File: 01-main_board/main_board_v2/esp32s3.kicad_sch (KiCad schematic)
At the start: 28 parts, among them IC10 ESP32-S3, Y1 ECS-400-10-37B2-CKY-TR, Y2 ECS-.327-12.5-34B-TR

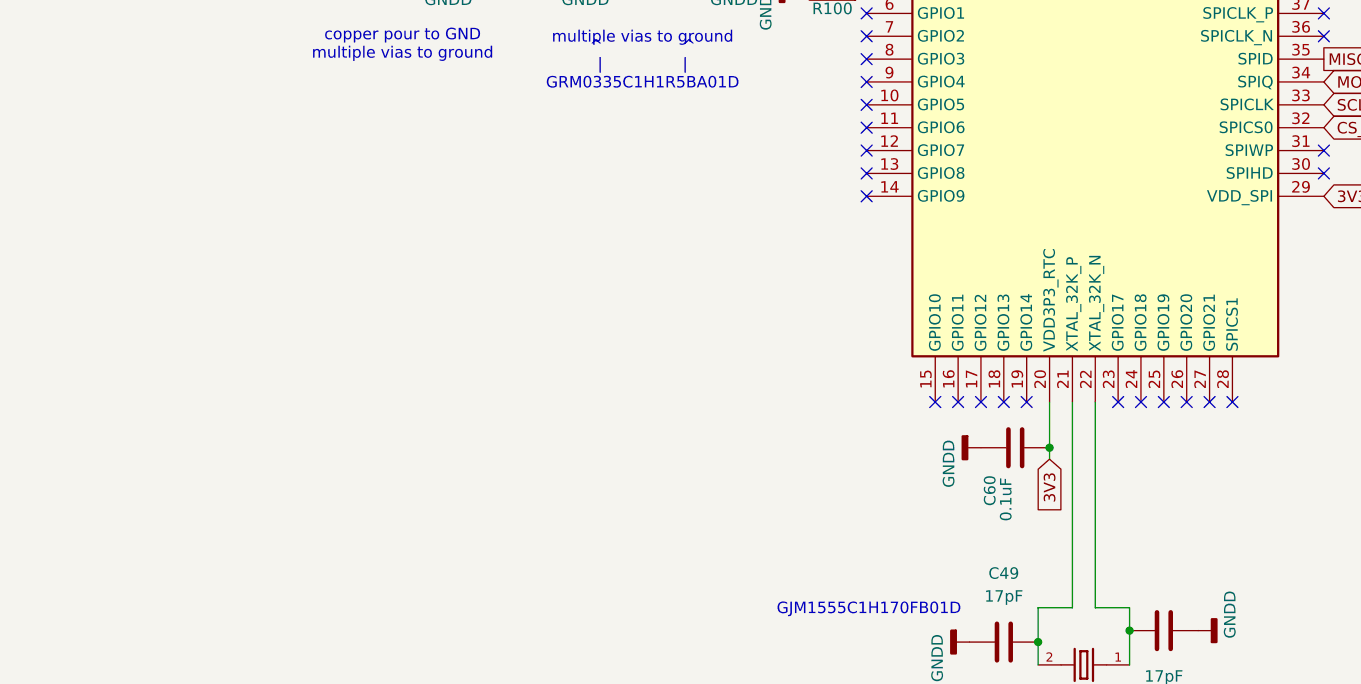
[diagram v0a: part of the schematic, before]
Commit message: added usb mux
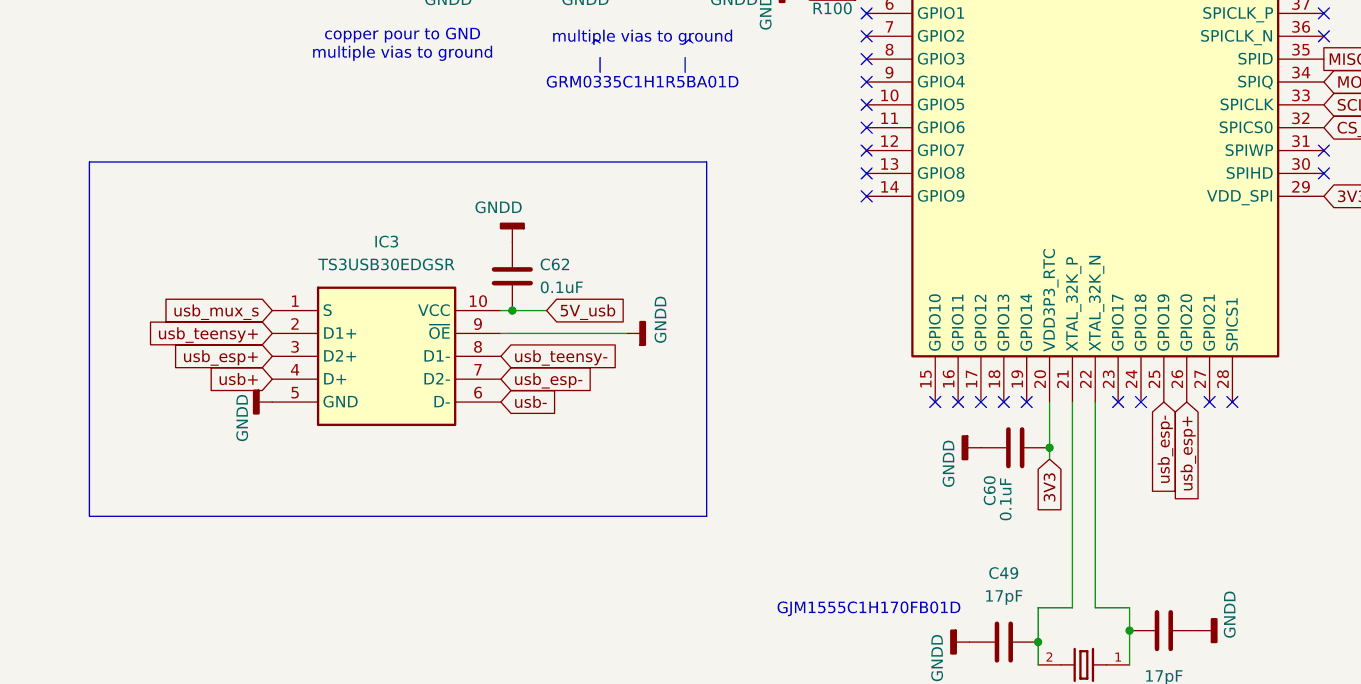
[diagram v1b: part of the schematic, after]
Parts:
- added C62: 0.1uF, Capacitor_SMD:C_0603_1608Metric, symbol Device:C
- added IC3: TS3USB30EDGSR, SOP50P490X110-10N, symbol 22XT_Main_v2:TS3USB30EDGSR
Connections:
- net GNDD: now also C62.1, IC3.5 (GND), IC3.9 (~{OE})
- net usb_esp-: now reaches IC10.25 (GPIO19)
- net usb_esp-: now also IC3.7 (D2-)
- net usb_esp+: now reaches IC10.26 (GPIO20)
- net usb_esp+: now also IC3.3 (D2+)
- new net 5V_usb: C62.2, IC3.10 (VCC)
- new net usb+: IC3.4 (D+)
- new net usb-: IC3.6 (D-)
- new net usb_mux_s: IC3.1 (S)
- new net usb_teensy+: IC3.2 (D1+)
- new net usb_teensy-: IC3.8 (D1-)
- no-connect marks 38 -> 36

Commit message: finished sensor input layout and some spi bus
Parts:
- C62: footprint Capacitor_SMD:C_0603_1608Metric -> Capacitor_SMD:C_0402_1005Metric
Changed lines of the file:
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@@
 			)
 		)
-		(property "Footprint" "Capacitor_SMD:C_0603_1608Metric"
+		(property "Footprint" "Capacitor_SMD:C_0402_1005Metric"
 			(at 82.2452 129.54 0)
 			(effects

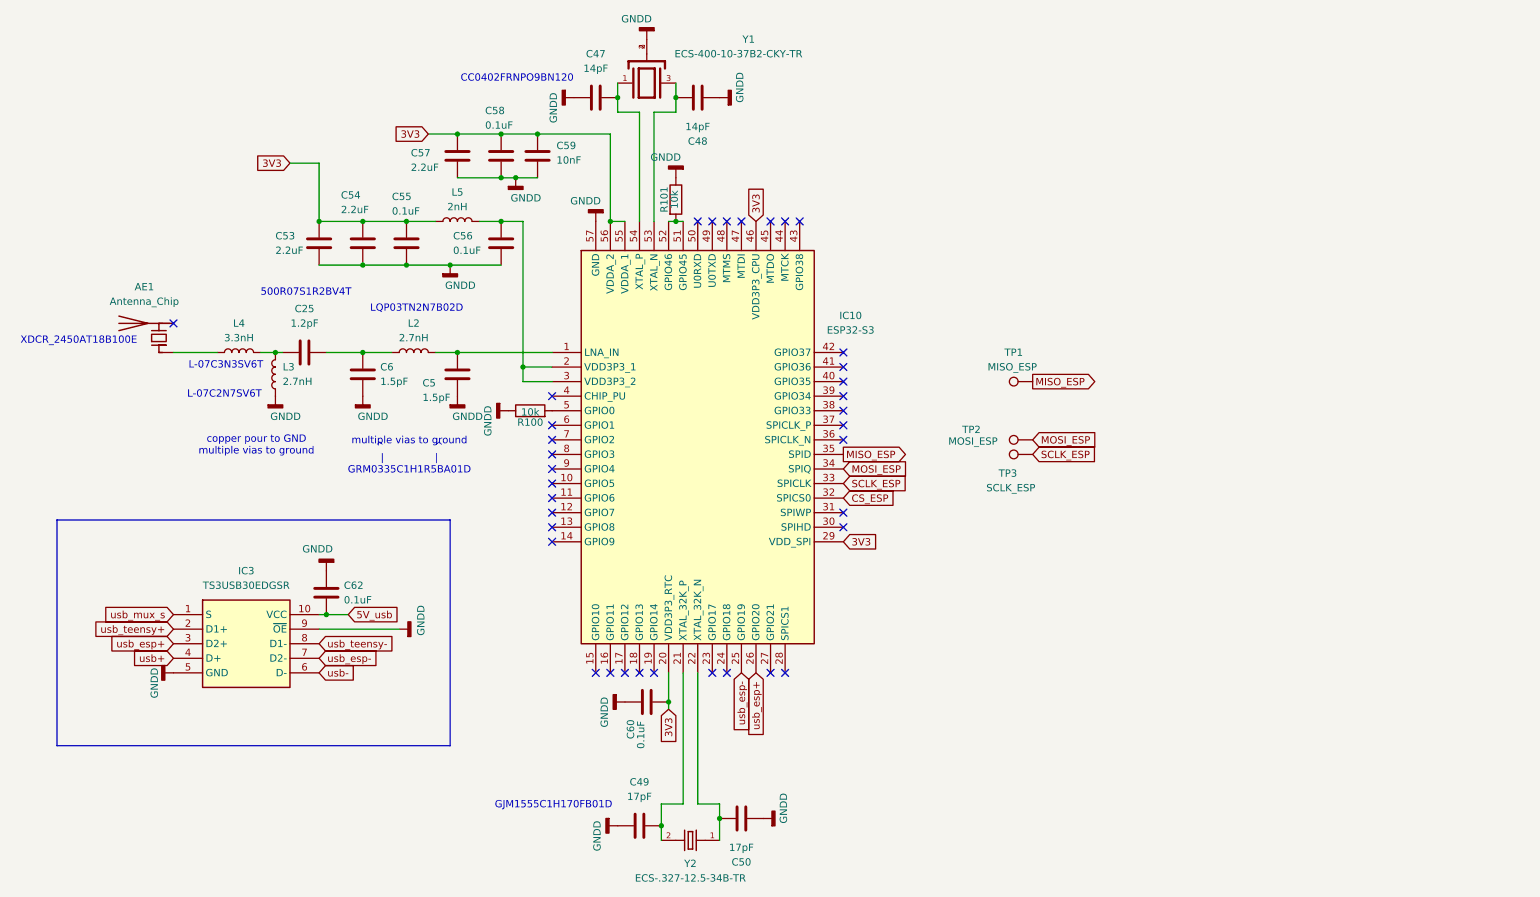
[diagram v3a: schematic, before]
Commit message: finished layout, resolved drc errors, need to resolve warnings and get checked
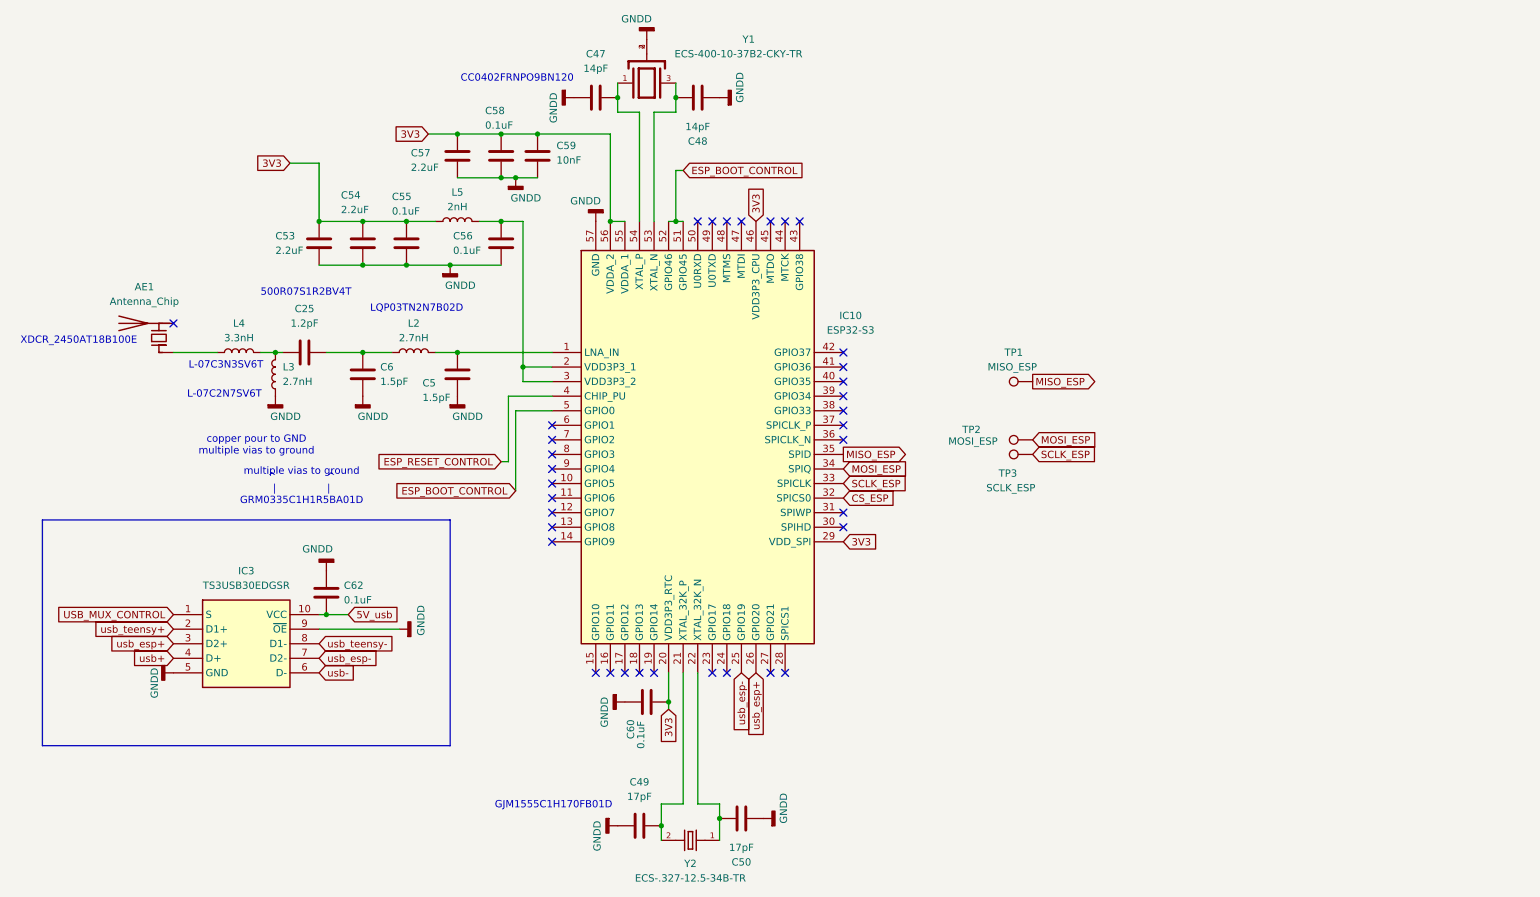
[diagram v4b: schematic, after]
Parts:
- removed R100, R101: 10k, Resistor_SMD:R_0402_1005Metric, symbol Device:R
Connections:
- net ESP_BOOT_CONTROL: now reaches IC10.5 (GPIO0)
- net ESP_BOOT_CONTROL: now also IC10.51 (GPIO45), IC10.52 (GPIO46)
- net ESP_RESET_CONTROL: now reaches IC10.4 (CHIP_PU)
- net usb_mux_s renamed USB_MUX_CONTROL
- no-connect marks 36 -> 35

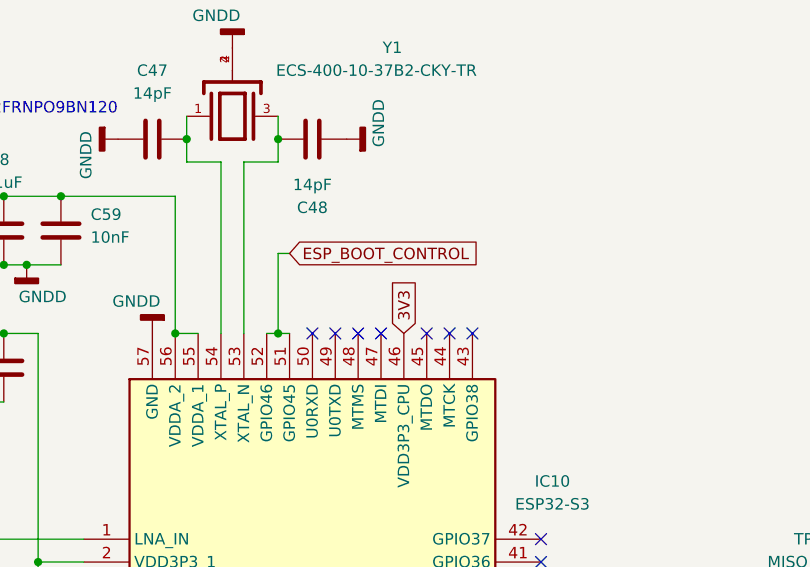
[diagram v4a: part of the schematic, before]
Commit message: resolved silkscreen issues, tied gpio45 to gnd
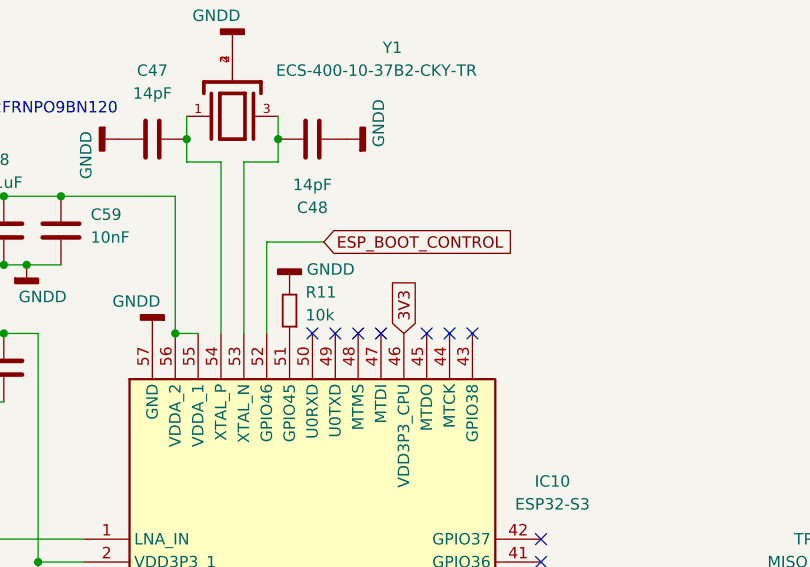
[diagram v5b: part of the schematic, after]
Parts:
- added R11: 10k, Resistor_SMD:R_0402_1005Metric, symbol Device:R_Small
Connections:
- net ESP_BOOT_CONTROL: no longer IC10.51 (GPIO45)
- net GNDD: now also R11.2
- new net: IC10.51 (GPIO45), R11.1
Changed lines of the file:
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@@
 	)
 	(junction
-		(at 142.24 60.96)
-		(diameter 0)
-		(color 0 0 0 0)
-	)
-	(junction
 		(at 104.14 83.82)
 		(diameter 0)
@@
 	(wire
 		(pts
-			(xy 142.24 60.96) (xy 143.51 60.96)
-		)
-		(stroke
-			(width 0)
-			(type default)
-		)
-	)
-	(wire
-		(pts
 			(xy 140.97 146.05) (xy 140.97 144.78)
 		)
@@
 	(wire
 		(pts
-			(xy 146.05 139.7) (xy 146.05 162.56)
-		)
-		(stroke
-			(width 0)
-			(type default)
-		)
-	)
-	(wire
-		(pts
-			(xy 115.57 86.36) (xy 120.65 86.36)
+			(xy 140.97 50.8) (xy 140.97 60.96)
 		)
 		(stroke
@@
 	(wire
 		(pts
-			(xy 143.51 139.7) (xy 143.51 162.56)
+			(xy 146.05 139.7) (xy 146.05 162.56)
 		)
 		(stroke
@@
 	(wire
 		(pts
-			(xy 142.24 60.96) (xy 142.24 52.07)
+			(xy 115.57 86.36) (xy 120.65 86.36)
 		)
 		(stroke
@@
 	(wire
 		(pts
-			(xy 140.97 60.96) (xy 142.24 60.96)
+			(xy 143.51 139.7) (xy 143.51 162.56)
 		)
 		(stroke
@@
 	(wire
 		(pts
-			(xy 142.24 52.07) (xy 143.51 52.07)
-		)
-		(stroke
-			(width 0)
-			(type default)
-		)
-	)
-	(wire
-		(pts
 			(xy 69.85 83.82) (xy 72.39 83.82)
 		)
@@
 	(wire
 		(pts
+			(xy 140.97 50.8) (xy 147.32 50.8)
+		)
+		(stroke
+			(width 0)
+			(type default)
+		)
+	)
+	(wire
+		(pts
 			(xy 149.86 168.91) (xy 149.86 165.1)
 		)
@@
 	(global_label "ESP_BOOT_CONTROL"
 		(shape input)
-		(at 143.51 52.07 0)
+		(at 147.32 50.8 0)
 		(fields_autoplaced yes)
 		(effects
@@
 		)
 		(property "Intersheetrefs" "${INTERSHEET_REFS}"
-			(at 165.4847 52.07 0)
+			(at 169.2947 50.8 0)
 			(effects
 				(font
@@
 	)
 	(symbol
+		(lib_id "Device:R_Small")
+		(at 143.51 58.42 180)
+		(unit 1)
+		(exclude_from_sim no)
+		(in_bom yes)
+		(on_board yes)
+		(dnp no)
+		(property "Reference" "R11"
+			(at 145.288 56.388 0)
+			(effects
+				(font
+					(size 1.27 1.27)
+				)
+				(justify right)
+			)
+		)
+		(property "Value" "10k"
+			(at 145.288 58.928 0)
+			(effects
+				(font
+					(size 1.27 1.27)
+				)
+				(justify right)
+			)
+		)
+		(property "Footprint" "Resistor_SMD:R_0402_1005Metric"
+			(at 143.51 58.42 0)
+			(effects
+				(font
+					(size 1.27 1.27)
+				)
+				(hide yes)
+			)
+		)
+		(property "Datasheet" "~"
+			(at 143.51 58.42 0)
+			(effects
+				(font
+					(size 1.27 1.27)
+				)
+				(hide yes)
+			)
+		)
+		(property "Description" "Resistor, small symbol"
+			(at 143.51 58.42 0)
+			(effects
+				(font
+					(size 1.27 1.27)
+				)
+				(hide yes)
+			)
+		)
+		(pin "1"
+		)
+		(pin "2"
+		)
+		(instances
+			(project "main_board_v2"
+				(path "/12c2237c-5932-49af-9119-92b28c846ae7/e5005576-746e-4110-9aa7-21d70d5867f0"
+					(reference "R11")
+					(unit 1)
+				)
+			)
+		)
+	)
+	(symbol
 		(lib_id "Device:C")
 		(at 135.89 166.37 270)
@@
 					(unit 1)
 				)
+			)
+		)
+	)
+	(symbol
+		(lib_id "power:GNDD")
+		(at 143.51 55.88 180)
+		(unit 1)
+		(exclude_from_sim no)
+		(in_bom yes)
+		(on_board yes)
+		(dnp no)
+		(property "Reference" "#PWR038"
+			(at 143.51 49.53 0)
+			(effects
+				(font
+					(size 1.27 1.27)
+				)
+				(hide yes)
+			)
+		)
+		(property "Value" "GNDD"
+			(at 148.082 53.848 0)
+			(effects
+				(font
+					(size 1.27 1.27)
+				)
+			)
+		)
+		(property "Footprint" ""
+			(at 143.51 55.88 0)
+			(effects
+				(font
+					(size 1.27 1.27)
+				)
+				(hide yes)
+			)
+		)
+		(property "Datasheet" ""
+			(at 143.51 55.88 0)
+			(effects
+				(font
+					(size 1.27 1.27)
+				)
+				(hide yes)
+			)
+		)
+		(property "Description" "Power symbol creates a global label with name \"GNDD\" , digital ground"
+			(at 143.51 55.88 0)
+			(effects
+				(font
+					(size 1.27 1.27)
+				)
+				(hide yes)
+			)
+		)
+		(pin "1"
+		)
+		(instances
+			(project "main_board_v2"
+				(path "/12c2237c-5932-49af-9119-92b28c846ae7/e5005576-746e-4110-9aa7-21d70d5867f0"
+					(reference "#PWR038")
+					(unit 1)
+				)

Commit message: added gpio3 tp
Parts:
- added TP14: GPIO3, TestPoint:TestPoint_Pad_1.0x1.0mm, symbol Connector:TestPoint
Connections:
- net at IC10.8 (GPIO3): now also TP14.1
- no-connect marks 35 -> 34
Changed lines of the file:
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@@
 	)
 	(no_connect
-		(at 120.65 101.6)
-	)
-	(no_connect
 		(at 133.35 139.7)
 	)
@@
 	(wire
 		(pts
+			(xy 116.84 101.6) (xy 116.84 116.84)
+		)
+		(stroke
+			(width 0)
+			(type default)
+		)
+	)
+	(wire
+		(pts
 			(xy 114.3 107.95) (xy 114.3 93.98)
 		)
@@
 	(wire
 		(pts
+			(xy 116.84 116.84) (xy 113.03 116.84)
+		)
+		(stroke
+			(width 0)
+			(type default)
+		)
+	)
+	(wire
+		(pts
 			(xy 149.86 162.56) (xy 146.05 162.56)
 		)
@@
 	(wire
 		(pts
+			(xy 120.65 101.6) (xy 116.84 101.6)
+		)
+		(stroke
+			(width 0)
+			(type default)
+		)
+	)
+	(wire
+		(pts
 			(xy 118.11 45.72) (xy 130.81 45.72)
 		)
@@
 					(unit 1)
 				)
+			)
+		)
+	)
+	(symbol
+		(lib_id "Connector:TestPoint")
+		(at 113.03 116.84 90)
+		(unit 1)
+		(exclude_from_sim no)
+		(in_bom yes)
+		(on_board yes)
+		(dnp no)
+		(property "Reference" "TP14"
+			(at 109.728 111.76 90)
+			(effects
+				(font
+					(size 1.27 1.27)
+				)
+			)
+		)
+		(property "Value" "GPIO3"
+			(at 109.474 114.3 90)
+			(effects
+				(font
+					(size 1.27 1.27)
+				)
+			)
+		)
+		(property "Footprint" "TestPoint:TestPoint_Pad_1.0x1.0mm"
+			(at 113.03 111.76 0)
+			(effects
+				(font
+					(size 1.27 1.27)
+				)
+				(hide yes)
+			)
+		)
+		(property "Datasheet" "~"
+			(at 113.03 111.76 0)
+			(effects
+				(font
+					(size 1.27 1.27)
+				)
+				(hide yes)
+			)
+		)
+		(property "Description" "test point"
+			(at 113.03 116.84 0)
+			(effects
+				(font
+					(size 1.27 1.27)
+				)
+				(hide yes)
+			)
+		)
+		(pin "1"
+		)
+		(instances
+			(project "main_board_v2"
+				(path "/12c2237c-5932-49af-9119-92b28c846ae7/e5005576-746e-4110-9aa7-21d70d5867f0"
+					(reference "TP14")
+					(unit 1)
+				)

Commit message: Finished preliminary routing
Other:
- note added: "GPIO0 and GPIO46: default pulled high for SPI Boot, button pulls low CHIP_PU (pin 4): default pulled high, button pulls low GPIO45: pulled down for 3V3 logic GPIO3: JTAG control, leave as NC b/c we are not using JTAGand are using USB OTG"
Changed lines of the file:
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@@
+		)
+	)
+	(text "GPIO0 and GPIO46: default pulled high for SPI Boot, button pulls low\n\nCHIP_PU (pin 4): default pulled high, button pulls low\n\nGPIO45: pulled down for 3V3 logic\n\nGPIO3: JTAG control, leave as NC b/c we are not using JTAGand are using USB OTG "
+		(exclude_from_sim no)
+		(at 193.294 64.516 0)
+		(effects
+			(font
+				(size 1.27 1.27)
+			)
+			(justify left)
 		)
 	)
